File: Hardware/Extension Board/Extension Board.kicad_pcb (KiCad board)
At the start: 2 copper layers, 20 parts, among them J1 ARDUINO_COMMS, J10 CNX_MODE, J11 CNX_TUNING, J12 CNX_I2C, J13 CNX_I2C, J14 CNX_SPI, J15 CNX_SD, J16 CNX_TFT, J2 ARDUINO_DIGITAL, J3 ARDUINO_ANALOG, J4 CNX_LED1, J5 CNX_LED2, J6 CNX_LED3, J7 CNX_LED4, J8 CNX_SPARE, J9 CNX_NEXT_AGAIN, U1 74HC14

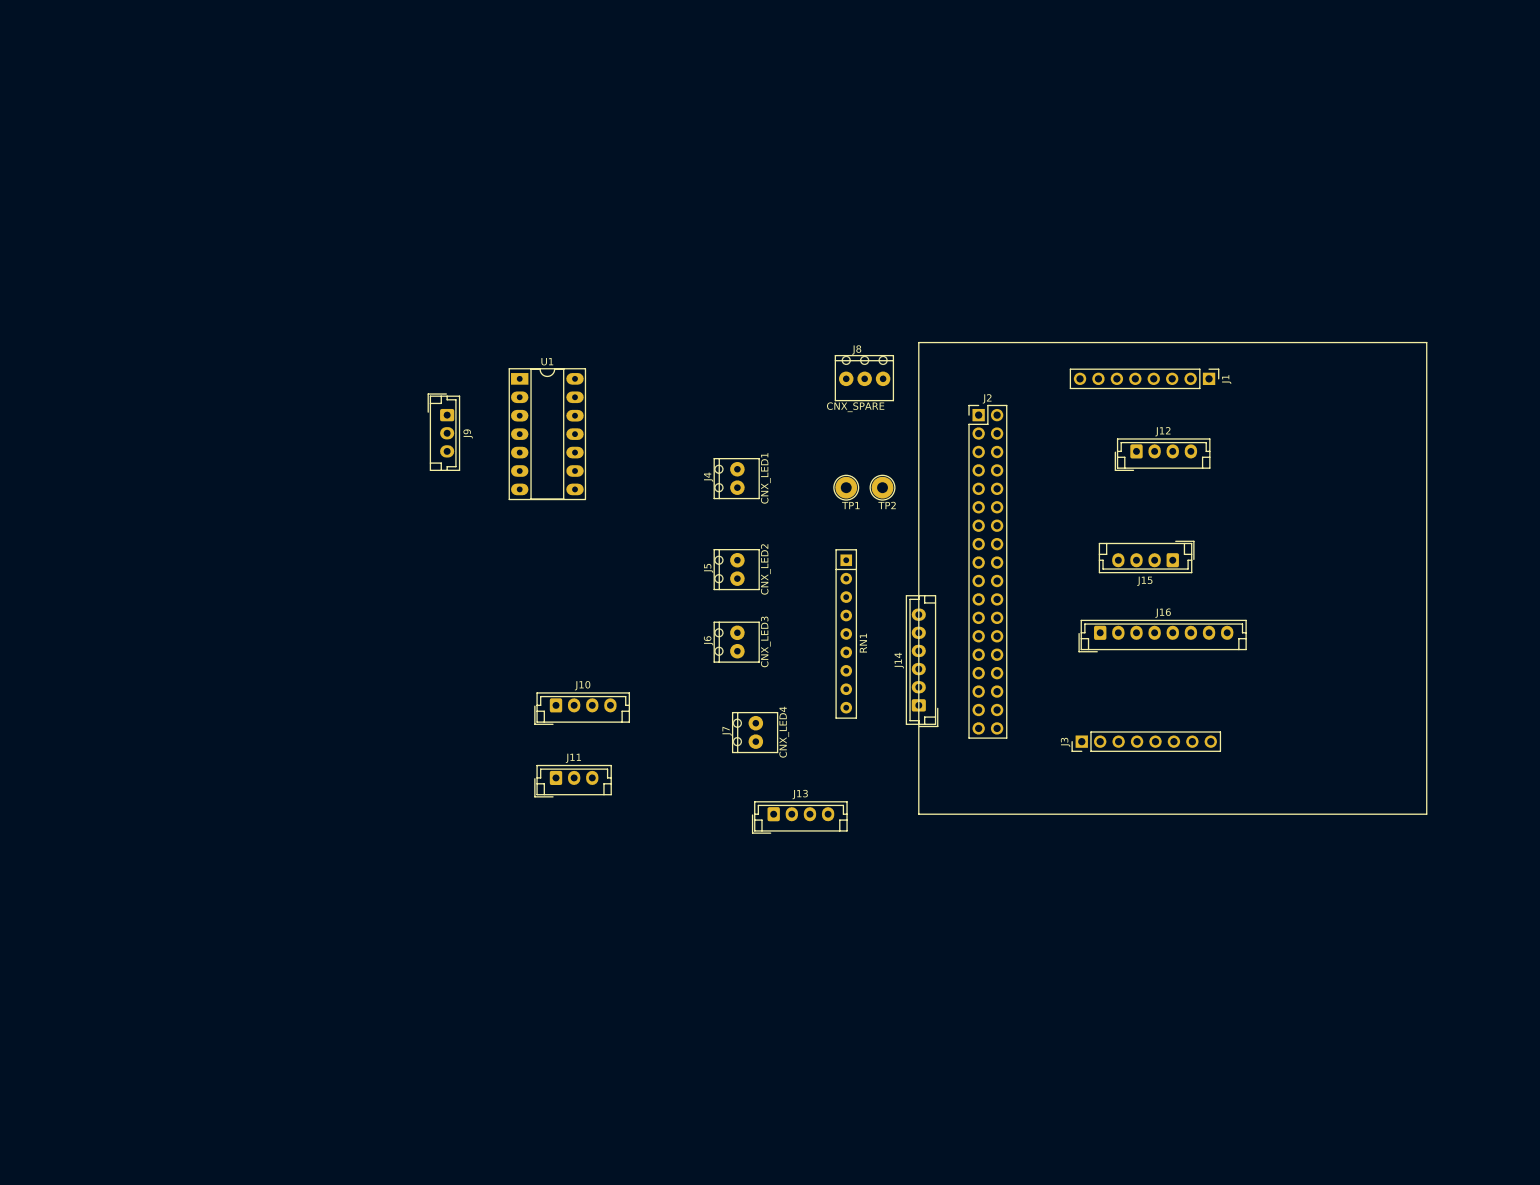
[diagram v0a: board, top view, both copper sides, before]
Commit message: PCB pour Extension board
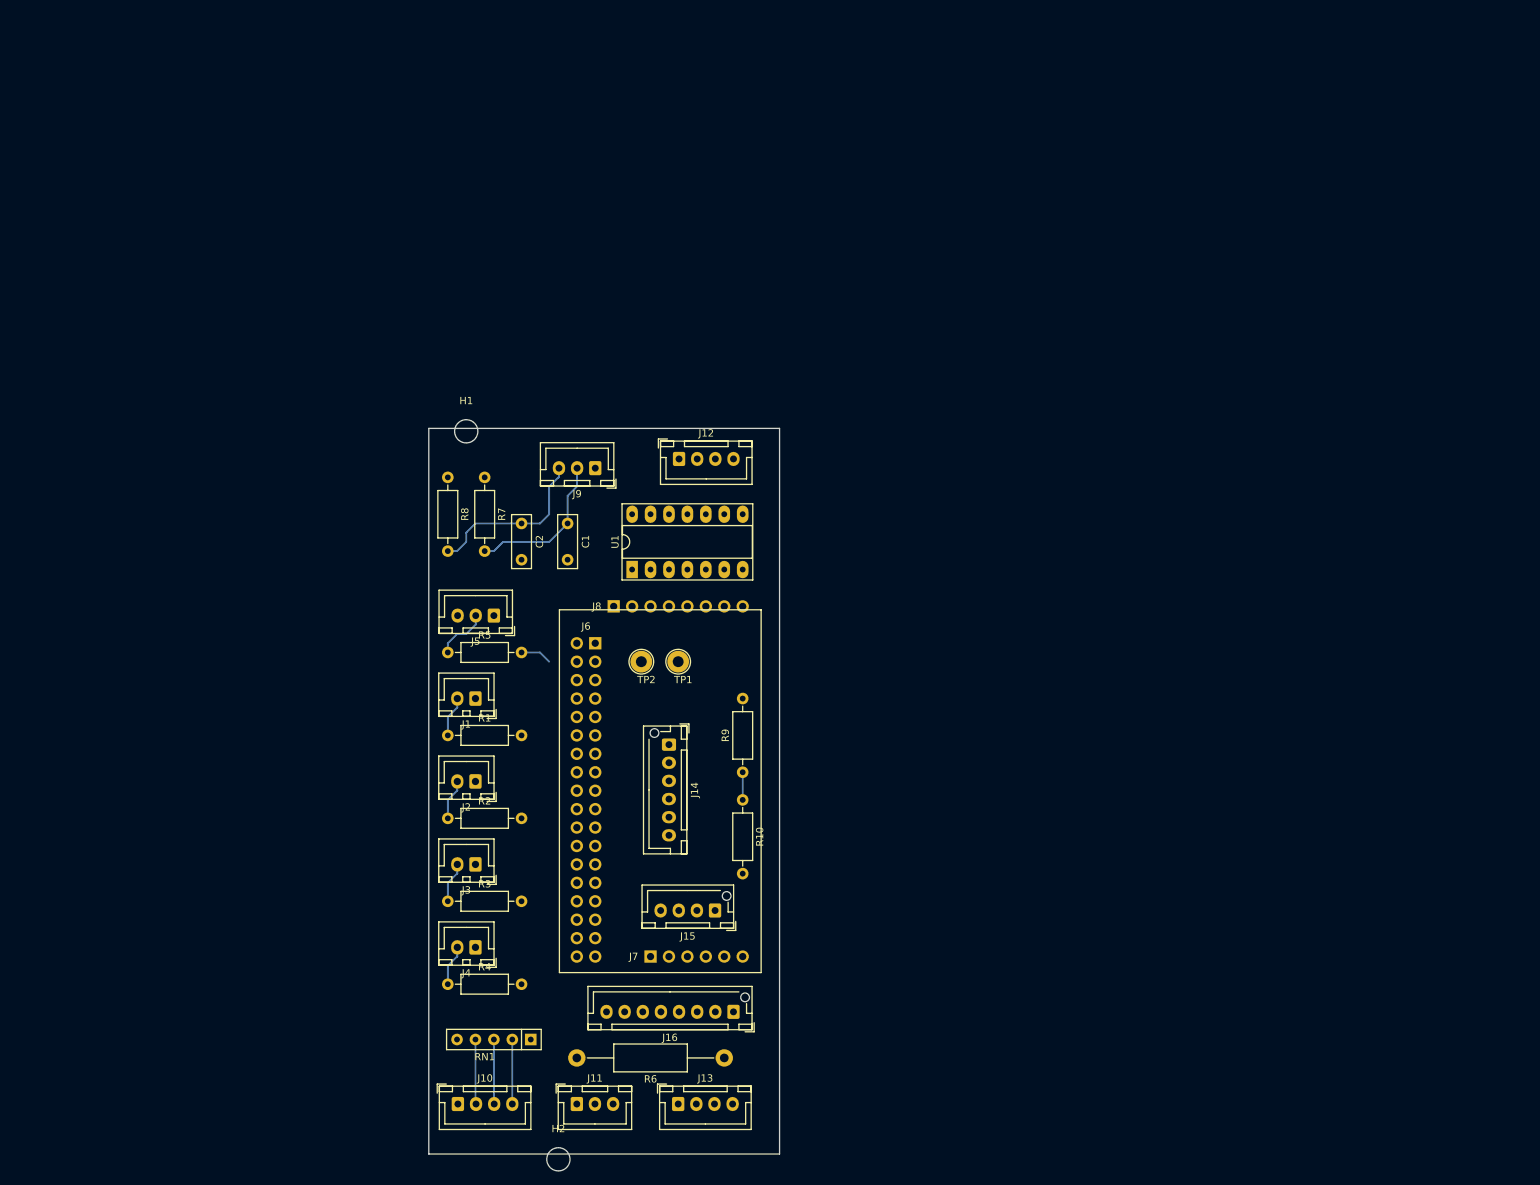
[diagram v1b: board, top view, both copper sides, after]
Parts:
- removed the J1 at (190.0, 55.0)
- removed the J5 at (125.0, 82.5)
- added C1: 10nF, Capacitor_THT:C_Rect_L7.2mm_W2.5mm_P5.00mm_FKS2_FKP2_MKS2_MKP2, F.Cu at (101.6, 74.9)
- added C2: 10nF, Capacitor_THT:C_Rect_L7.2mm_W2.5mm_P5.00mm_FKS2_FKP2_MKS2_MKP2, F.Cu at (95.2, 74.9)
- added H1: MountingHole, MountingHole:MountingHole_3.2mm_M3, F.Cu at (87.6, 62.2)
- added H2: MountingHole, MountingHole:MountingHole_3.2mm_M3, F.Cu at (100.3, 162.6)
- added J3: CNX_LED, Connector_JST:JST_XH_B2B-XH-A_1x02_P2.50mm_Vertical, F.Cu at (88.9, 121.9)
- added J7: ARDUINO_COMMS, Connector_PinHeader_2.54mm:PinHeader_1x06_P2.54mm_Vertical, B.Cu at (113.0, 134.6)
- added R1: 200, Resistor_THT:R_Axial_DIN0207_L6.3mm_D2.5mm_P10.16mm_Horizontal, F.Cu at (85.1, 104.1)
- added R10: 90k, Resistor_THT:R_Axial_DIN0207_L6.3mm_D2.5mm_P10.16mm_Horizontal, F.Cu at (125.7, 113.0)
- added R2: 200, Resistor_THT:R_Axial_DIN0207_L6.3mm_D2.5mm_P10.16mm_Horizontal, F.Cu at (85.1, 115.6)
- added R3: 200, Resistor_THT:R_Axial_DIN0207_L6.3mm_D2.5mm_P10.16mm_Horizontal, F.Cu at (85.1, 127.0)
- added R4: 200, Resistor_THT:R_Axial_DIN0207_L6.3mm_D2.5mm_P10.16mm_Horizontal, F.Cu at (85.1, 138.4)
- added R5: 200, Resistor_THT:R_Axial_DIN0207_L6.3mm_D2.5mm_P10.16mm_Horizontal, F.Cu at (85.1, 92.7)
- added R6: A CALCULER, Resistor_THT:R_Axial_DIN0411_L9.9mm_D3.6mm_P20.32mm_Horizontal, F.Cu at (123.2, 148.6)
- added R7: 4.7k, Resistor_THT:R_Axial_DIN0207_L6.3mm_D2.5mm_P10.16mm_Horizontal, F.Cu at (90.2, 68.6)
- added R8: 4.7k, Resistor_THT:R_Axial_DIN0207_L6.3mm_D2.5mm_P10.16mm_Horizontal, F.Cu at (85.1, 68.6)
- added R9: 50k, Resistor_THT:R_Axial_DIN0207_L6.3mm_D2.5mm_P10.16mm_Horizontal, F.Cu at (125.7, 109.2)
- J1: renamed from J7; value CNX_LED4 -> CNX_LED; footprint MesModules:Bloc_de_jonction_CI-MPT_2.54mm_01x02 -> Connector_JST:JST_XH_B2B-XH-A_1x02_P2.50mm_Vertical
- J10, J12, J13: footprint Connector_JST:JST_EH_B4B-EH-A_1x04_P2.50mm_Vertical -> Connector_JST:JST_XH_B4B-XH-A_1x04_P2.50mm_Vertical
- J11, J9: footprint Connector_JST:JST_EH_B3B-EH-A_1x03_P2.50mm_Vertical -> Connector_JST:JST_XH_B3B-XH-A_1x03_P2.50mm_Vertical
- J14: footprint Connector_JST:JST_EH_B6B-EH-A_1x06_P2.50mm_Vertical -> Connector_JST:JST_XH_B6B-XH-AM_1x06_P2.50mm_Vertical
- J15: footprint Connector_JST:JST_EH_B4B-EH-A_1x04_P2.50mm_Vertical -> Connector_JST:JST_XH_B4B-XH-AM_1x04_P2.50mm_Vertical
- J16: footprint Connector_JST:JST_EH_B8B-EH-A_1x08_P2.50mm_Vertical -> Connector_JST:JST_XH_B8B-XH-AM_1x08_P2.50mm_Vertical
- J2: renamed from J6; value CNX_LED3 -> CNX_LED; footprint MesModules:Bloc_de_jonction_CI-MPT_2.54mm_01x02 -> Connector_JST:JST_XH_B2B-XH-A_1x02_P2.50mm_Vertical
- J4: value CNX_LED1 -> CNX_LED; footprint MesModules:Bloc_de_jonction_CI-MPT_2.54mm_01x02 -> Connector_JST:JST_XH_B2B-XH-A_1x02_P2.50mm_Vertical
- J5: renamed from J8; footprint MesModules:Bloc_de_jonction_CI-MPT_2.54mm_01x03 -> Connector_JST:JST_XH_B3B-XH-A_1x03_P2.50mm_Vertical
- J6: renamed from J2; moved to B.Cu
- J8: renamed from J3; moved to B.Cu
- RN1: footprint Resistor_THT:R_Array_SIP9 -> Resistor_THT:R_Array_SIP5
- moved J15 79.4 mm to (121.9, 128.3)
- moved RN1 79.1 mm to (96.5, 146.1), turned to 180 degrees
- moved J4 72.9 mm to (88.9, 133.3), turned to 180 degrees
- moved J16 72.7 mm to (124.5, 142.2), turned to 180 degrees
- moved J8 67.1 mm to (108.0, 86.4), turned to 270 degrees
- moved J12 63.0 mm to (117.0, 66.0)
- moved J6 61.5 mm to (105.4, 91.4), turned to 180 degrees
- moved J5 58.5 mm to (91.4, 87.6), turned to 180 degrees
- moved J10 56.6 mm to (86.5, 154.9)
- moved J11 45.0 mm to (102.9, 154.9)
- moved J13 42.1 mm to (116.8, 154.9)
- moved TP2 41.0 mm to (111.8, 94.0)
- moved J2 40.3 mm to (88.9, 110.5), turned to 180 degrees
- moved J1 39.1 mm to (88.9, 99.1), turned to 180 degrees
- moved J14 34.9 mm to (115.6, 105.4), turned to 270 degrees
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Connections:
- net D27 renamed Net-(J6-Pad8)
- net D43 renamed Net-(J6-Pad24)
- J10 pad 1: Net-(J10-Pad1) -> GND
- J10 pad 2: Net-(J10-Pad2) -> D29
- J10 pad 3: Net-(J10-Pad3) -> D31
- J10 pad 4: GND -> D33
- J11 pad 1: A12 -> A14
- J11 pad 2: A14 -> A12
- J12 pad 2: SDA -> SCL
- J12 pad 3: SCL -> SDA
- J13 pad 2: SDA -> SCL
- J13 pad 3: SCL -> SDA
- J14 pad 2: MISO -> D48
- J14 pad 4: SCK -> MISO
- J14 pad 5: D49 -> SCK
- J15 pad 1: D41 -> D40
- J16 pad 4: D23 -> D16
- J16 pad 5: D25 -> D17
- J16 pad 6: D35 -> D42
- J6 pad 10: Net-(J10-Pad1) -> D29
- J6 pad 12: Net-(J10-Pad2) -> D31
- J6 pad 14: Net-(J10-Pad3) -> D33
- J6 pad 16: D35 -> Net-(J6-Pad16)
- J6 pad 21: Net-(J2-Pad21) -> D40
- J6 pad 22: D41 -> Net-(J6-Pad22)
- J6 pad 23: Net-(J2-Pad23) -> D42
- J6 pad 29: Net-(J2-Pad29) -> D48
- J6 pad 30: D49 -> Net-(J6-Pad30)
- J8 pad 2: Net-(J3-Pad2) -> A14
- J8 pad 4: Net-(J3-Pad4) -> A12
- J8 pad 5: A12 -> Net-(J8-Pad5)
- J8 pad 7: A14 -> Net-(J8-Pad7)
- J9 pad 1: Net-(C1-Pad1) -> GND
- J9 pad 2: Net-(C2-Pad1) -> Net-(C1-Pad1)
- J9 pad 3: GND -> Net-(C2-Pad1)
- RN1 pad 2: Net-(J10-Pad1) -> D33
- RN1 pad 3: Net-(J10-Pad2) -> D31
- RN1 pad 4: Net-(J10-Pad3) -> D29
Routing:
- net Net-(C2-Pad1): track 0.00 -> 23.7 mm
- net Net-(C1-Pad1): track 0.00 -> 21.2 mm
- net D29: track 0.00 -> 8.92 mm
- net D31: track 0.00 -> 8.91 mm
- net D33: track 0.00 -> 8.89 mm
- net Net-(J5-Pad2): track 0.00 -> 7.42 mm
- net Net-(J4-Pad2): track 0.00 -> 5.63 mm
- net Net-(J3-Pad2): track 0.00 -> 5.63 mm
- net Net-(J1-Pad2): track 0.00 -> 5.63 mm
- net Net-(J2-Pad2): track 0.00 -> 5.63 mm
- net D23: track 0.00 -> 4.34 mm
- net /TFT_LED: track 0.00 -> 3.81 mm
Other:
- board outline added: 48.3 x 100 mm

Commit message: PCB Extension board
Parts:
- J1, J2, J3, J4: moved to B.Cu
- J10: value CNX_MODE -> MODE
- J11: value CNX_TUNING -> TUNING
- J12, J13: value CNX_I2C -> I2C
- J14: value CNX_SPI -> SPI; moved to B.Cu
- J15: value CNX_SD -> SD
- J16: value CNX_TFT -> TFT
- J5: value CNX_SPARE -> SPARE; moved to B.Cu
- J9: value CNX_NEXT_AGAIN -> NEXT_AGAIN
- moved H2 135.3 mm to (34.3, 44.5), turned to 180 degrees
- moved RN1 113.4 mm to (33.0, 52.1), turned to 0 degrees
- moved R6 109.6 mm to (157.5, 44.5)
- moved J10 94.7 mm to (67.3, 62.2), turned to 180 degrees
- moved J13 94.3 mm to (76.2, 69.8), turned to 270 degrees
- moved J11 94.3 mm to (143.5, 69.8), turned to 270 degrees
- moved J4 89.3 mm to (80.0, 44.5)
- moved R4 88.2 mm to (74.9, 50.8)
- moved U1 78.7 mm to (33.0, 67.3)
- moved J3 77.5 mm to (91.4, 44.5)
- moved J14 76.8 mm to (67.3, 45.7), turned to 180 degrees
- moved R3 76.3 mm to (88.9, 50.8)
- moved J7 74.5 mm to (83.8, 66.0), turned to 180 degrees
- moved J16 73.7 mm to (121.9, 68.6)
- moved H1 69.7 mm to (156.8, 54.0), turned to 180 degrees
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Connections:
- U1 pad 2: D18 -> D19
- U1 pad 4: D19 -> D18
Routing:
- net VCC: track 0.00 -> 278.2 mm, vias 0 -> 1
- net GND: track 0.00 -> 160.6 mm
- net SDA: track 0.00 -> 115.1 mm
- net SCL: track 0.00 -> 112.0 mm
- net D19: track 0.00 -> 74.2 mm
- net D44: track 0.00 -> 66.1 mm, vias 0 -> 2
- net D18: track 0.00 -> 65.7 mm
- net A12: track 0.00 -> 57.6 mm
- net A14: track 0.00 -> 36.7 mm
- net D17: track 0.00 -> 33.4 mm, vias 0 -> 1
- net D46: track 0.00 -> 28.8 mm
- net D33: track 8.89 -> 33.6 mm
- net D31: track 8.91 -> 33.6 mm
- net D29: track 8.92 -> 33.6 mm
- net Net-(C1-Pad1): track 21.2 -> 43.1 mm
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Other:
- board size 48.3 x 100 mm -> 135.9 x 44.4 mm
- net class Power added: clearance 0.2, trace_width 0.4, via_dia 0.8, via_drill 0.4
- board text added: "5V"
- board text added: "GND"
- board text added: "LEDs"
- board text added: "SPARE"

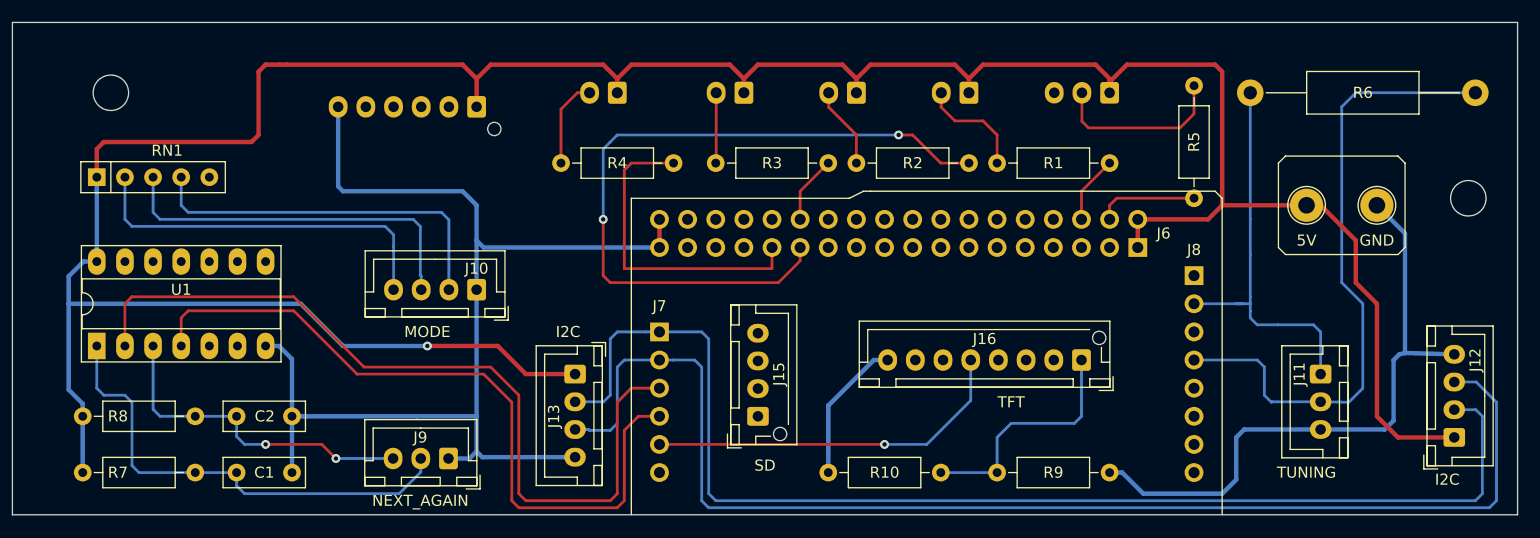
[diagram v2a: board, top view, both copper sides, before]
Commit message: PCB Layout complete
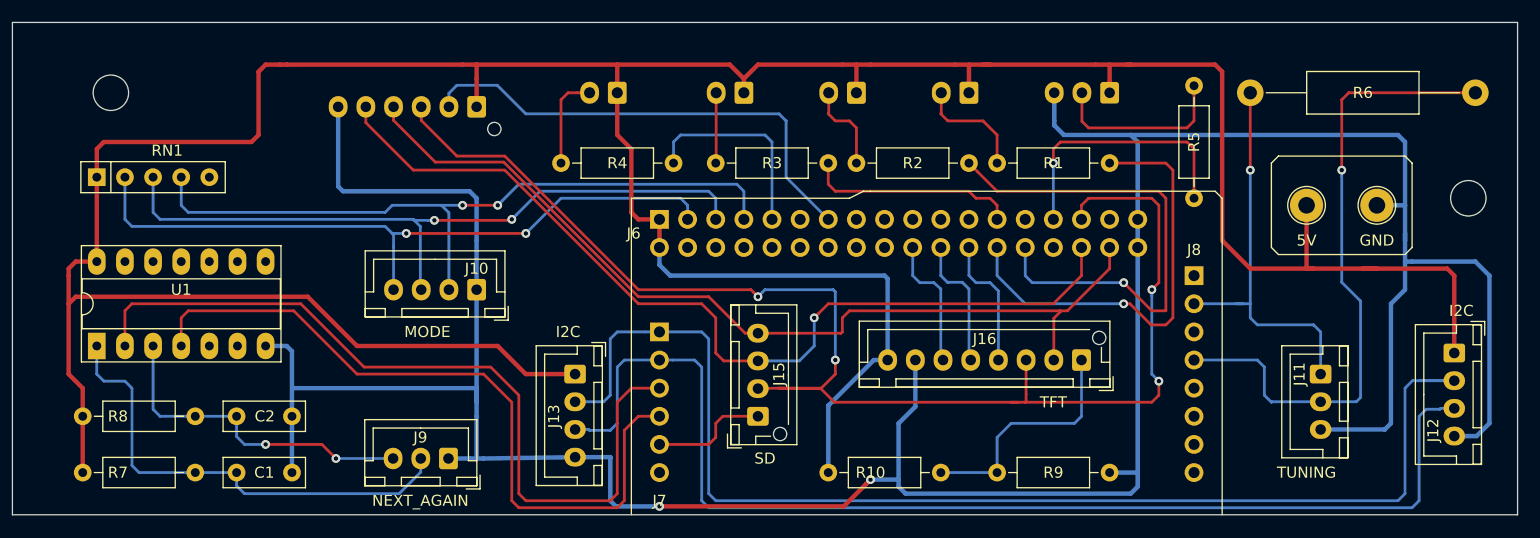
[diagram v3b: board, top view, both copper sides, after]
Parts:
- moved J6 43.3 mm to (83.8, 55.9), turned to 270 degrees
- moved J12 7.62 mm to (155.6, 67.9), turned to 270 degrees
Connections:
- J10 pad 2: D29 -> D27
- J10 pad 3: D31 -> D25
- J10 pad 4: D33 -> D23
- J14 pad 2: D48 -> D33
- J14 pad 4: MISO -> SCK
- J14 pad 5: SCK -> MISO
- J15 pad 1: D40 -> D17
- J16 pad 4: D16 -> D42
- J16 pad 5: D17 -> D40
- J16 pad 6: D42 -> D38
- J6 pad 10: D29 -> Net-(J6-Pad10)
- J6 pad 12: D31 -> Net-(J6-Pad12)
- J6 pad 13: Net-(J6-Pad13) -> D33
- J6 pad 14: D33 -> Net-(J6-Pad14)
- J6 pad 20: Net-(J6-Pad20) -> D38
- J6 pad 21: D40 -> Net-(J6-Pad21)
- J6 pad 22: Net-(J6-Pad22) -> D40
- J6 pad 23: D42 -> Net-(J6-Pad23)
- J6 pad 24: Net-(J6-Pad24) -> D42
- J6 pad 25: D44 -> D45
- J6 pad 26: D45 -> D44
- J6 pad 27: D46 -> Net-(J6-Pad27)
- J6 pad 28: Net-(J6-Pad28) -> D46
- J6 pad 29: D48 -> D49
- J6 pad 3: Net-(J6-Pad3) -> D23
- J6 pad 31: MISO -> MOSI
- J6 pad 32: MOSI -> MISO
- J6 pad 33: SCK -> Net-(J6-Pad33)
- J6 pad 34: Net-(J6-Pad34) -> SCK
- J6 pad 4: D23 -> Net-(J6-Pad4)
- J6 pad 5: Net-(J6-Pad5) -> D25
- J6 pad 6: D25 -> Net-(J6-Pad6)
- J6 pad 7: Net-(J6-Pad7) -> D27
- J6 pad 9: Net-(J6-Pad9) -> D29
- J7 pad 6: D16 -> Net-(J7-Pad6)
- R1 pad 2: D25 -> D44
- R2 pad 2: D44 -> D46
- R4 pad 2: D46 -> D29
- R5 pad 2: D23 -> D49
- RN1 pad 2: D33 -> D23
- RN1 pad 3: D31 -> D25
- RN1 pad 4: D29 -> D27
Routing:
- net MOSI: track 0.00 -> 126.5 mm, vias 0 -> 4
- net GND: track 160.6 -> 285.6 mm, vias 0 -> 2
- net MISO: track 0.00 -> 84.0 mm, vias 0 -> 1
- net SCK: track 0.00 -> 83.6 mm
- net D27: track 0.00 -> 65.4 mm, vias 0 -> 2
- net D25: track 6.13 -> 64.2 mm, vias 0 -> 2
- net D23: track 9.15 -> 63.1 mm, vias 0 -> 2
- net VCC: track 278.2 -> 319.3 mm, vias 1 -> 0
- net D31: track 33.6 -> 0.00 mm
- net D44: track 66.1 -> 39.8 mm, vias 2 -> 1
- net D49: track 0.00 -> 24.0 mm, vias 0 -> 1
- net D17: track 33.4 -> 10.7 mm, vias 1 -> 0
- net D46: track 28.8 -> 45.8 mm, vias 0 -> 1
- net D29: track 33.6 -> 18.3 mm
- net D45: track 6.13 -> 19.2 mm
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
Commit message: PCB updated.
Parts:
- moved J9 0.64 mm to (64.8, 76.8)
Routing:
- net Net-(C1-Pad1): track 43.1 -> 44.1 mm
- net GND: track 285.6 -> 285.1 mm
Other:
- board size 135.9 x 44.4 mm -> 132.7 x 44.4 mm
